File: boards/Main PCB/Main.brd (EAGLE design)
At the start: 160 x 101.3 mm, 41 parts, among them CN1 MINIB, IC1 FT232RL, Q1 BSS138, Q2 BSS138, U1 MIC5225-3.3, Y1 32.768kHz

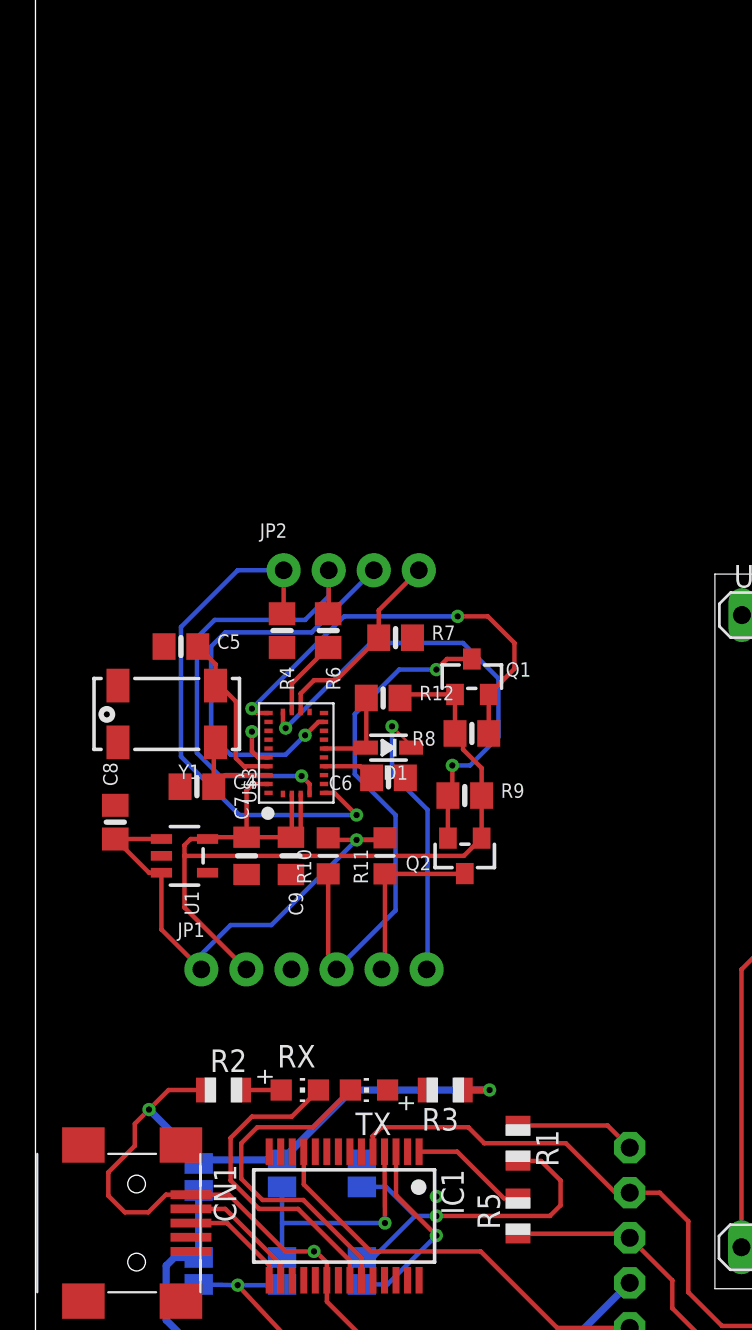
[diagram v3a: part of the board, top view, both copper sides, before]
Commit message: Updating boaard file and removing settings from git
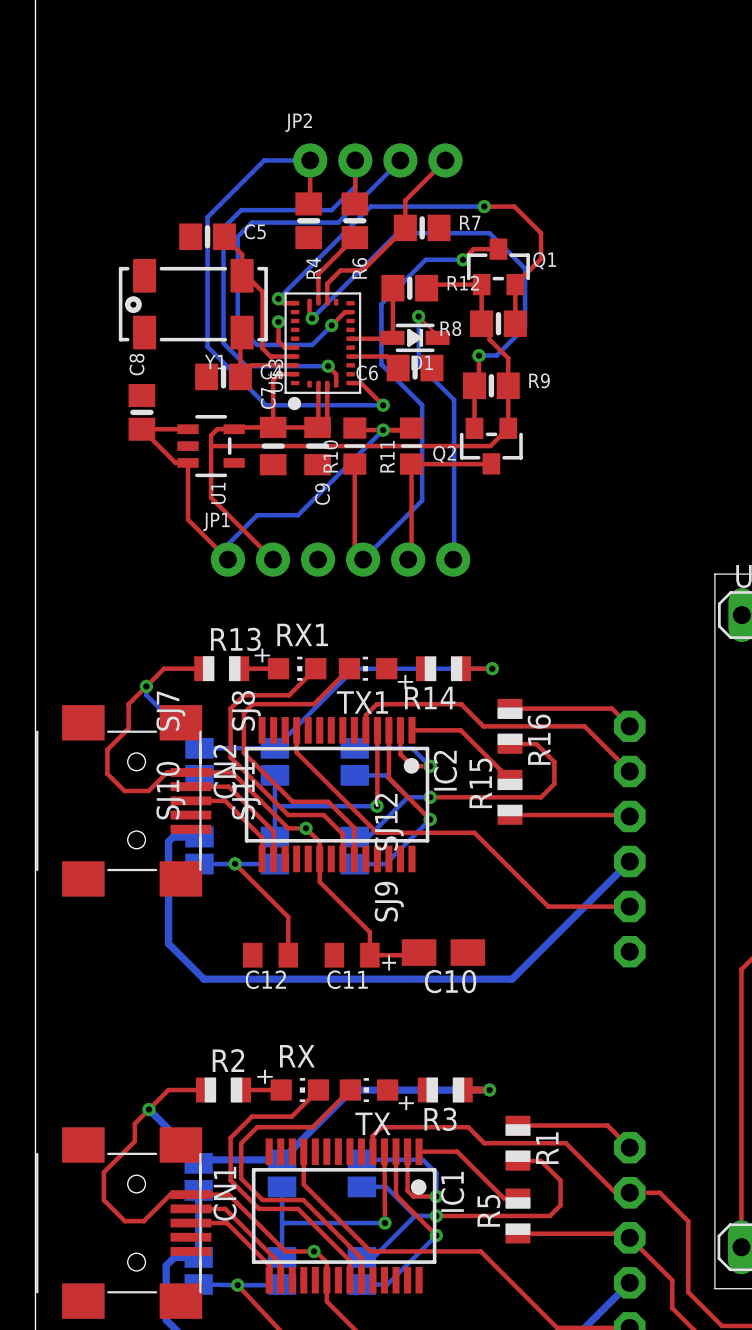
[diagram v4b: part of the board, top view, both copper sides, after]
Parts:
- added C10: 10uF, adafruit:A/3216-18R
- added C11, C12: 0.1uF, adafruit:C0805K
- added CN2: MINIB, adafruit:USB-MINIB
- added FTDI1: (no value), adafruit:1X06-CLEANBIG
- added IC2: FT232RL, ftdichip:SSOP28
- added R13, R14: 1K, adafruit:R0805
- added R15, R16: 10, adafruit:R0805
- added RX1: Green, adafruit:CHIP-LED0805
- added SJ10, SJ11, SJ12, SJ7, SJ8, SJ9: (no value), jumper:SJ
- added TX1: Red, adafruit:CHIP-LED0805
- moved JP2 23.1 mm to (19.3, 72.9)
- moved Q1 23.1 mm to (26.1, 66.9)
- moved C4 23.1 mm to (10.6, 60.7)
- moved C6 23.1 mm to (21.4, 61.2)
- moved C8 23.1 mm to (6.00, 58.7)
- moved D1 23.1 mm to (21.4, 62.9)
- moved R12 23.1 mm to (21.1, 65.7)
- moved R4 23.1 mm to (15.4, 69.5)
- moved R6 23.1 mm to (18.0, 69.5)
- moved R8 23.1 mm to (26.1, 63.7)
- moved R9 23.1 mm to (25.7, 60.2)
- moved U$3 23.1 mm to (16.2, 62.6)
- moved JP1 23.1 mm to (17.2, 50.4)
- moved C5 23.1 mm to (9.70, 68.6)
- moved C7 23.1 mm to (13.4, 56.8)
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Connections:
- new net +3V3_2: C12.1, IC2.17, SJ10.2, SJ11.2
- new net +5V_2: C10.+, C11.1, CN2.VBUS, IC2.20, R13.1, R14.1, SJ7.1, SJ8.1
- new net CTS2: FTDI1.2, IC2.11
- new net DTR2: IC2.2, SJ12.2
- new net N$12: CN2.D+, IC2.15
- new net N$13: CN2.D-, IC2.16
- new net N$14: IC2.23, TX1.C
- new net N$15: IC2.22, RX1.C
- new net N$16: R13.2, RX1.A
- new net N$17: R14.2, TX1.A
- new net N$18: IC2.1, R15.2
- new net N$19: FTDI1.6, R16.1
- new net RTS2: IC2.3, SJ9.1
- new net RTSDTR2: R16.2, SJ12.1, SJ9.2
- new net RX2: FTDI1.5, IC2.5
- new net TX2: FTDI1.4, R15.1
- new net VCCIO2: IC2.4, SJ11.1, SJ8.2
- new net VCCOUT2: FTDI1.3, SJ10.1, SJ7.2
- net GND: now also C10.-, C11.2, C12.2, CN2.GND, FTDI1.1, IC2.18, IC2.21, IC2.25, IC2.26, IC2.7
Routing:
- net +5V_2: track 0.00 -> 59.1 mm, vias 0 -> 3
- net VCCOUT2: track 0.00 -> 37.2 mm
- net CTS2: track 0.00 -> 23.6 mm
- net RTSDTR2: track 0.00 -> 20.2 mm, vias 0 -> 1
- net N$14: track 0.00 -> 19.0 mm
- net N$15: track 0.00 -> 18.0 mm
- net RX2: track 0.00 -> 17.6 mm
- net VCCIO2: track 0.00 -> 13.5 mm, vias 0 -> 1
- net RTS2: track 0.00 -> 11.3 mm, vias 0 -> 1
- net +3V3_2: track 0.00 -> 10.6 mm, vias 0 -> 1
- net DTR: track 0.00 -> 9.78 mm
- net DTR2: track 0.00 -> 7.97 mm, vias 0 -> 1
- net N$13: track 0.00 -> 7.26 mm
- net N$19: track 0.00 -> 7.16 mm
- net TX2: track 0.00 -> 6.78 mm
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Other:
- board text added: "C1"
- board text added: "C10"
- board text added: "C11"
- board text added: "C12"
- board text added: "C2"
- board text added: "C3"
- board text added: "C4"
- board text added: "C5"
- board text added: "C6"
- board text added: "C7"
- board text added: "C8"
- board text added: "C9"
- board text added: "CN1"
- board text added: "CN2"
- board text added: "D1"
- board text added: "FTDI"
- board text added: "FTDI1"
- board text added: "IC1"
- board text added: "IC2"
- board text added: "JP1"
- board text added: "JP2"
- board text added: "Q1"
- board text added: "Q2"
- board text added: "R1"
- board text added: "R10"
- board text added: "R11"
- board text added: "R12"
- board text added: "R13"
- board text added: "R14"
- board text added: "R15"
- board text added: "R16"
- board text added: "R2"
- board text added: "R3"
- board text added: "R4"
- board text added: "R5"
- board text added: "R6"
- board text added: "R7"
- board text added: "R8"
- board text added: "R9"
- board text added: "RX"
- board text added: "RX1"
- board text added: "SJ1"
- board text added: "SJ10"
- board text added: "SJ11"
- board text added: "SJ12"
- board text added: "SJ2"
- board text added: "SJ3"
- board text added: "SJ4"
- board text added: "SJ5"
- board text added: "SJ6"
- board text added: "SJ7"
- board text added: "SJ8"
- board text added: "SJ9"
- board text added: "TX"
- board text added: "TX1"
- board text added: "U$1"
- board text added: "U$3"
- board text added: "U1"
- board text added: "Y1"

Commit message: Updating current board for review
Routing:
- net VCCOUT2: track 37.2 -> 36.2 mm
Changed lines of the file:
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@@
 <contactref element="CN1" pad="D+"/>
 <contactref element="IC1" pad="15"/>
-<wire x1="10.8" y1="13" x2="13.175" y2="10.625" width="0.254" layer="1"/>
-<wire x1="13.175" y1="10.625" x2="13.175" y2="9.775" width="0.254" layer="1"/>
-<wire x1="8.764" y1="13" x2="10.8" y2="13" width="0.254" layer="1"/>
+<wire x1="10.55" y1="13" x2="13.175" y2="10.375" width="0.254" layer="1"/>
+<wire x1="13.175" y1="10.375" x2="13.175" y2="9.775" width="0.254" layer="1"/>
+<wire x1="8.764" y1="13" x2="10.55" y2="13" width="0.254" layer="1"/>
 </signal>
 <signal name="N$4">
@@
 <wire x1="15.65" y1="18.4" x2="12.5" y2="18.4" width="0.254" layer="1"/>
 <wire x1="12.5" y1="18.4" x2="11.6" y2="17.5" width="0.254" layer="1"/>
-<wire x1="11.6" y1="17.5" x2="11.6" y2="15.5" width="0.254" layer="1"/>
-<wire x1="11.6" y1="15.5" x2="12.8" y2="14.3" width="0.254" layer="1"/>
-<wire x1="12.8" y1="14.3" x2="15.1" y2="14.3" width="0.254" layer="1"/>
-<wire x1="15.1" y1="14.3" x2="18.4" y2="11" width="0.254" layer="1"/>
+<wire x1="11.6" y1="17.5" x2="11.6" y2="15.75" width="0.254" layer="1"/>
+<wire x1="11.6" y1="15.75" x2="14.8" y2="12.55" width="0.254" layer="1"/>
+<wire x1="14.8" y1="12.55" x2="16.85" y2="12.55" width="0.254" layer="1"/>
+<wire x1="16.85" y1="12.55" x2="18.4" y2="11" width="0.254" layer="1"/>
 <wire x1="18.4" y1="11" x2="18.4" y2="9.8" width="0.254" layer="1"/>
 <wire x1="18.4" y1="9.8" x2="18.375" y2="9.775" width="0.254" layer="1"/>
@@
 <wire x1="12.2" y1="19" x2="11" y2="17.8" width="0.254" layer="1"/>
 <wire x1="11" y1="17.8" x2="11" y2="15.4" width="0.254" layer="1"/>
-<wire x1="11" y1="15.4" x2="12.6" y2="13.8" width="0.254" layer="1"/>
-<wire x1="12.6" y1="13.8" x2="14.8" y2="13.8" width="0.254" layer="1"/>
+<wire x1="11" y1="15.4" x2="14.35" y2="12.05" width="0.254" layer="1"/>
+<wire x1="14.35" y1="12.05" x2="16.55" y2="12.05" width="0.254" layer="1"/>
 <wire x1="17.725" y1="10.875" x2="17.725" y2="9.775" width="0.254" layer="1"/>
 <wire x1="14.45" y1="19" x2="12.2" y2="19" width="0.254" layer="1"/>
-<wire x1="14.8" y1="13.8" x2="17.725" y2="10.875" width="0.254" layer="1"/>
+<wire x1="16.55" y1="12.05" x2="17.725" y2="10.875" width="0.254" layer="1"/>
 </signal>
 <signal name="N$8">
@@
 <wire x1="5.6" y1="18.6" x2="5.6" y2="17.60284375" width="0.254" layer="1"/>
 <wire x1="3.857" y1="15.85984375" x2="3.857" y2="14.29015625" width="0.254" layer="1"/>
-<wire x1="3.857" y1="14.29015625" x2="5.04015625" y2="13.107" width="0.254" layer="1"/>
-<wire x1="5.04015625" y1="13.107" x2="6.10984375" y2="13.107" width="0.254" layer="1"/>
+<wire x1="3.857" y1="14.29015625" x2="4.79015625" y2="13.357" width="0.254" layer="1"/>
+<wire x1="4.79015625" y1="13.357" x2="6.35984375" y2="13.357" width="0.254" layer="1"/>
 <wire x1="7.60284375" y1="14.6" x2="8.764" y2="14.6" width="0.254" layer="1"/>
-<wire x1="6.10984375" y1="13.107" x2="7.60284375" y2="14.6" width="0.254" layer="1"/>
+<wire x1="6.35984375" y1="13.357" x2="7.60284375" y2="14.6" width="0.254" layer="1"/>
 <wire x1="5.6" y1="17.60284375" x2="3.857" y2="15.85984375" width="0.254" layer="1"/>
 <wire x1="8.764" y1="14.6" x2="10.9" y2="14.6" width="0.254" layer="1"/>
@@
 <contactref element="IC1" pad="5"/>
 <contactref element="FTDI" pad="5"/>
-<wire x1="33.5" y1="14.71" x2="32.69" y2="14.71" width="0.254" layer="1"/>
-<wire x1="32.69" y1="14.71" x2="29.9" y2="17.5" width="0.254" layer="1"/>
-<wire x1="29.9" y1="17.5" x2="25.3" y2="17.5" width="0.254" layer="1"/>
+<wire x1="33.5" y1="14.71" x2="33.44" y2="14.71" width="0.254" layer="1"/>
+<wire x1="33.44" y1="14.71" x2="30.65" y2="17.5" width="0.254" layer="1"/>
+<wire x1="30.65" y1="17.5" x2="25.3" y2="17.5" width="0.254" layer="1"/>
 <wire x1="25.3" y1="17.5" x2="24.4" y2="18.4" width="0.254" layer="1"/>
 <wire x1="24.4" y1="18.4" x2="19.5" y2="18.4" width="0.254" layer="1"/>
@@
 <contactref element="SJ6" pad="2"/>
 <via x="22.6" y="14.5" extent="1-16" drill="0.35"/>
-<wire x1="22.6" y1="14.5" x2="21.3" y2="14.5" width="0.254" layer="1"/>
-<wire x1="20.975" y1="14.825" x2="20.975" y2="17.025" width="0.254" layer="1"/>
-<wire x1="21.3" y1="14.5" x2="20.975" y2="14.825" width="0.254" layer="1"/>
+<wire x1="22.6" y1="14.5" x2="21.8" y2="14.5" width="0.254" layer="1"/>
+<wire x1="20.975" y1="15.325" x2="20.975" y2="17.025" width="0.254" layer="1"/>
+<wire x1="21.8" y1="14.5" x2="20.975" y2="15.325" width="0.254" layer="1"/>
 <wire x1="22.6" y1="14.5" x2="22.6" y2="15.8" width="0.254" layer="16"/>
 <wire x1="22.6" y1="15.8" x2="21.838" y2="16.562" width="0.254" layer="16"/>
@@
 <wire x1="9.2" y1="11.062" x2="7.8312" y2="11.062" width="0.4064" layer="16"/>
 <wire x1="7.8312" y1="11.062" x2="7.3692" y2="10.6" width="0.4064" layer="16"/>
-<wire x1="7.3692" y1="10.6" x2="7.3692" y2="7.5308" width="0.4064" layer="16"/>
-<wire x1="7.3692" y1="7.5308" x2="11.5" y2="3.4" width="0.4064" layer="16"/>
-<wire x1="11.5" y1="3.4" x2="21" y2="3.4" width="0.4064" layer="16"/>
-<wire x1="21" y1="3.4" x2="27.27" y2="3.4" width="0.4064" layer="16"/>
+<wire x1="7.3692" y1="10.6" x2="7.3692" y2="7.0308" width="0.4064" layer="16"/>
+<wire x1="7.3692" y1="7.0308" x2="11" y2="3.4" width="0.4064" layer="16"/>
+<wire x1="11" y1="3.4" x2="27.27" y2="3.4" width="0.4064" layer="16"/>
 <wire x1="27.27" y1="3.4" x2="33.5" y2="9.63" width="0.4064" layer="16"/>
 <wire x1="9.2" y1="11.062" x2="9.2" y2="14.838" width="0.4064" layer="16"/>
@@
 <wire x1="9.25" y1="34.762" x2="7.762" y2="34.762" width="0.4064" layer="16"/>
 <wire x1="7.762" y1="34.762" x2="7.5" y2="34.5" width="0.4064" layer="16"/>
-<wire x1="7.5" y1="34.5" x2="7.5" y2="28.75" width="0.4064" layer="16"/>
-<wire x1="7.5" y1="28.75" x2="9.5" y2="26.75" width="0.4064" layer="16"/>
-<wire x1="9.5" y1="26.75" x2="26.87" y2="26.75" width="0.4064" layer="16"/>
+<wire x1="7.5" y1="34.5" x2="7.5" y2="30.5" width="0.4064" layer="16"/>
+<wire x1="7.5" y1="30.5" x2="11.25" y2="26.75" width="0.4064" layer="16"/>
+<wire x1="11.25" y1="26.75" x2="26.87" y2="26.75" width="0.4064" layer="16"/>
 <wire x1="26.87" y1="26.75" x2="33.5" y2="33.38" width="0.4064" layer="16"/>
 <wire x1="9.25" y1="34.762" x2="9.25" y2="38.238" width="0" layer="19" extent="16-16"/>
@@
 <wire x1="9.25" y1="39.762" x2="6.25" y2="42.762" width="0.254" layer="16"/>
 <wire x1="6.25" y1="42.762" x2="6.25" y2="43.25" width="0.254" layer="16"/>
-<wire x1="9.25" y1="39.762" x2="13.5" y2="39.762" width="0.254" layer="16"/>
+<wire x1="9.25" y1="39.762" x2="13.5" y2="39.762" width="0.4064" layer="16"/>
 <wire x1="8.764" y1="38.4" x2="11.1" y2="38.4" width="0.254" layer="1"/>
 <wire x1="11.1" y1="38.4" x2="14.25" y2="35.25" width="0.254" layer="1"/>
@@
 <wire x1="16.025" y1="32.225" x2="18.85" y2="29.4" width="0.254" layer="1"/>
 <via x="25.75" y="44.25" extent="1-16" drill="0.35"/>
-<wire x1="24" y1="44.25" x2="25.75" y2="44.25" width="0.254" layer="1"/>
-<wire x1="25.75" y1="44.25" x2="17.988" y2="44.25" width="0.254" layer="16"/>
-<wire x1="17.988" y1="44.25" x2="13.5" y2="39.762" width="0.254" layer="16"/>
+<wire x1="24" y1="44.25" x2="25.75" y2="44.25" width="0.4064" layer="1"/>
+<wire x1="25.75" y1="44.25" x2="17.988" y2="44.25" width="0.4064" layer="16"/>
+<wire x1="17.988" y1="44.25" x2="13.5" y2="39.762" width="0.4064" layer="16"/>
 </signal>
 <signal name="+3V3_2">

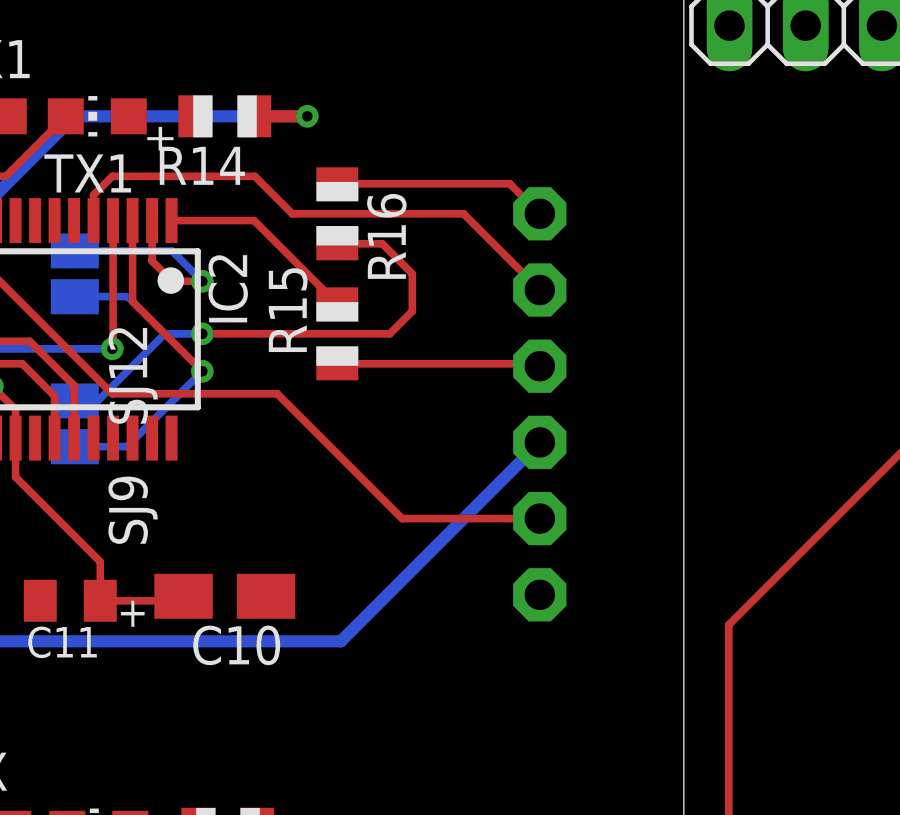
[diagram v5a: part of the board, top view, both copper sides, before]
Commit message: Fixing mirrored FTDI on reverse of board
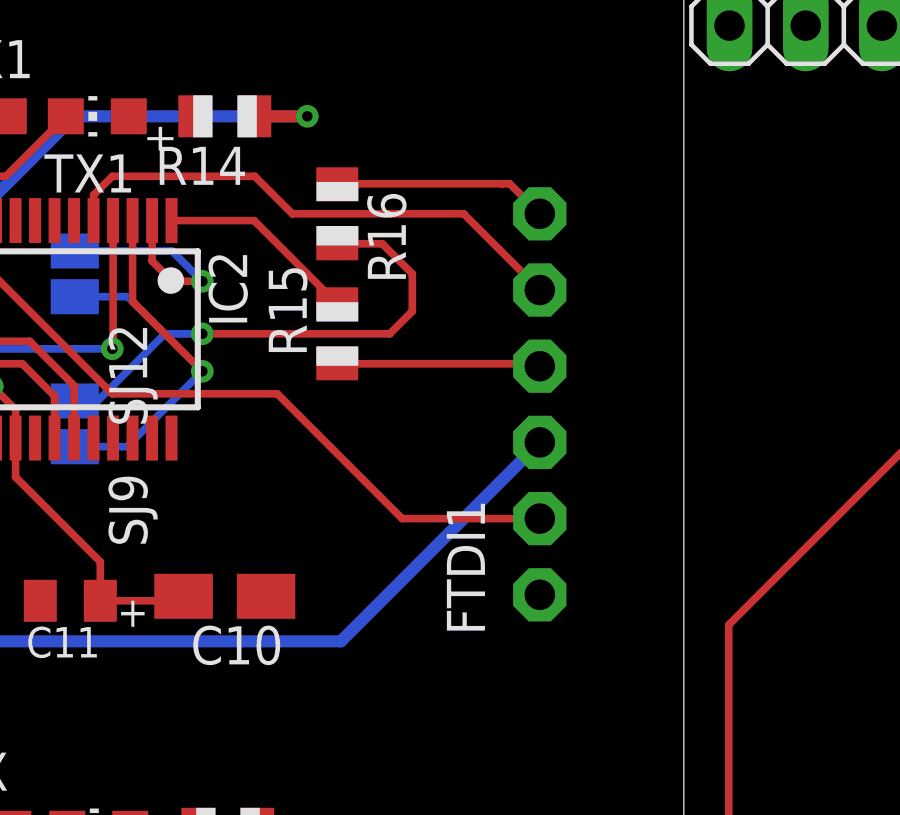
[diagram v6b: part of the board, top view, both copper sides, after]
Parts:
- flipped FTDI1 to the top
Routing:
- net TX2: vias 0 -> 1
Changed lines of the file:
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@@
 <drawing>
 <settings>
-<setting alwaysvectorfont="no"/>
+<setting alwaysvectorfont="yes"/>
 <setting verticaltext="up"/>
 </settings>
@@
 </layers>
 <board>
+<fusionsync huburn="a.cGVyc29uYWw6dWUyYTZiNjY2" projecturn="a.cGVyc29uYWw6dWUyYTZiNjY2I0QyMDE4MDEyNjExNDM0NjI1Ng" f3durn="urn:adsk.wipprod:dm.lineage:n0fbRr_KT-25qyjz7S21eg" pcbguid="6d30f37e-4e16-49f5-a01d-9dac6a8f2f00" lastpulledtime="" lastsyncedchangeguid="4fb3dc34-9c1d-74fe-b5d9-68b589e5fe3c"/>
 <plain>
 <wire x1="0" y1="0" x2="160" y2="0" width="0" layer="20"/>
@@
 <text x="24.000003125" y="58.900009375" size="0.8128" layer="125" ratio="18" rot="R180">D1</text>
 <text x="31.671209375" y="3.203803125" size="1.27" layer="125" ratio="10" rot="R90">FTDI</text>
-<text x="31.75" y="28.75" size="1.27" layer="125" ratio="10" rot="R90">FTDI1</text>
+<text x="31.75" y="27" size="1.27" layer="125" ratio="10" rot="R90">FTDI1</text>
 <text x="22.876003125" y="16.029890625" size="1.27" layer="125" rot="R270">IC1</text>
 <text x="20.42400625" y="41.370103125" size="1.27" layer="125" rot="R90">IC2</text>
@@
 <attribute name="VALUE" x="18" y="39.4001" size="0.02" layer="28" rot="MR90"/>
 </element>
-<element name="FTDI1" library="adafruit" package="1X06-CLEANBIG" value="" x="33.5" y="34.65" smashed="yes" rot="MR90">
-<attribute name="NAME" x="35.3288" y="26.9538" size="1.27" layer="26" ratio="10" rot="MR90"/>
-<attribute name="VALUE" x="30.325" y="27.03" size="1.27" layer="28" rot="MR90"/>
+<element name="FTDI1" library="adafruit" package="1X06-CLEANBIG" value="" x="33.5" y="34.65" smashed="yes" rot="R90">
+<attribute name="NAME" x="31.6712" y="26.9538" size="1.27" layer="25" ratio="10" rot="R90"/>
+<attribute name="VALUE" x="36.675" y="27.03" size="1.27" layer="27" rot="R90"/>
 </element>
 <element name="R16" library="adafruit" package="R0805" value="10" x="26.75" y="41" smashed="yes" rot="R270">
@@
 <contactref element="R16" pad="1"/>
 <contactref element="FTDI1" pad="6"/>
-<wire x1="26.75" y1="42" x2="32.5" y2="42" width="0.254" layer="1"/>
+<wire x1="26.75" y1="42" x2="32.25" y2="42" width="0.254" layer="1"/>
+<wire x1="32.25" y1="42" x2="32.5" y2="42" width="0.254" layer="1"/>
 <wire x1="32.5" y1="42" x2="33.5" y2="41" width="0.254" layer="1"/>
 </signal>
@@
 <wire x1="14.725" y1="39.525" x2="19.25" y2="35" width="0.254" layer="1"/>
 <wire x1="19.25" y1="35" x2="24.75" y2="35" width="0.254" layer="1"/>
+<wire x1="24.75" y1="35" x2="28.91" y2="30.84" width="0.254" layer="1"/>
 <wire x1="28.91" y1="30.84" x2="33.5" y2="30.84" width="0.254" layer="1"/>
-<wire x1="24.75" y1="35" x2="28.91" y2="30.84" width="0.254" layer="1"/>
 </signal>
 <signal name="TX2">
@@
 <contactref element="R15" pad="1"/>
 <wire x1="26.75" y1="36" x2="33.42" y2="36" width="0.254" layer="1"/>
-<wire x1="33.42" y1="36" x2="33.5" y2="35.92" width="0.254" layer="1"/>
+<wire x1="33.42" y1="36" x2="33.5" y2="35.92" width="0.254" layer="16"/>
+<via x="33.42" y="36" extent="1-16" drill="0.35"/>
 </signal>
 <signal name="RX2">
@@
 <wire x1="19.25" y1="42.25" x2="24" y2="42.25" width="0.254" layer="1"/>
 <wire x1="24" y1="42.25" x2="25.25" y2="41" width="0.254" layer="1"/>
+<wire x1="25.25" y1="41" x2="30.96" y2="41" width="0.254" layer="1"/>
 <wire x1="30.96" y1="41" x2="33.5" y2="38.46" width="0.254" layer="1"/>
-<wire x1="25.25" y1="41" x2="30.96" y2="41" width="0.254" layer="1"/>
 </signal>
 <signal name="RTSDTR2">
@@
 </note>
 <note version="8.3" severity="warning">
+Since Version 8.3, EAGLE supports Fusion synchronisation.
+This feature will not be available in this version and saving
+the document will break the link to the Fusion PCB feature.
+</note>
+<note version="8.3" severity="warning">
